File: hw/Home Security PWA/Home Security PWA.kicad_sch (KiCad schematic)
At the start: 46 parts, among them J1 Conn_01x10_Pin, J10 1884340000, J11 1884340000, J12 1884340000, J13 1884340000, J14 1884340000, J15 1884340000, J16 1884340000, J17 1884340000, J18 1884340000, J19 1884340000, J2 Conn_01x10_Pin, J20 1884340000, J21 1884340000, J22 1884340000, J23 1884340000, J24 1884340000, J25 1884340000, J26 1884340000, J27 1884340000, J28 1884340000, J29 1884340000, J3 1884340000, J30 1884340000, J4 1884340000, J5 1884340000, J6 1884340000, J7 1884340000, J8 1884340000, J9 1884340000, U1 ADS1115IDGS, U2 ADS1115IDGS, U3 MCP23017_SO

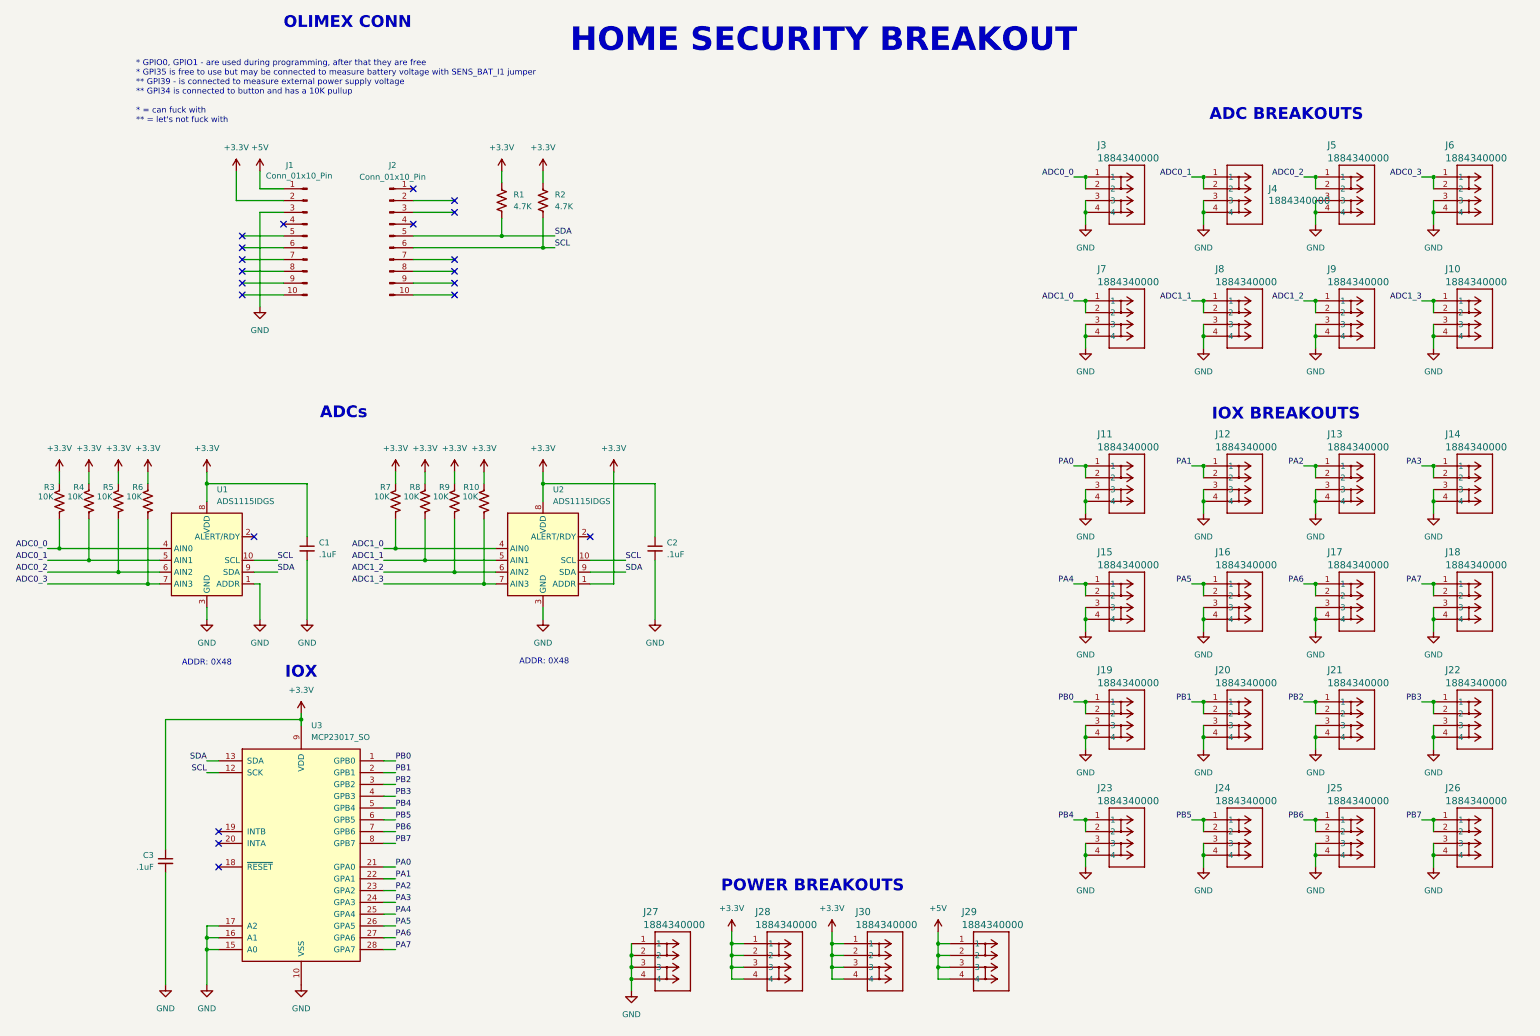
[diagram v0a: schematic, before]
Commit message: Rev A.
Added these "top" loader cable holders.
Added GPIOs that directly attach to the ESP32.
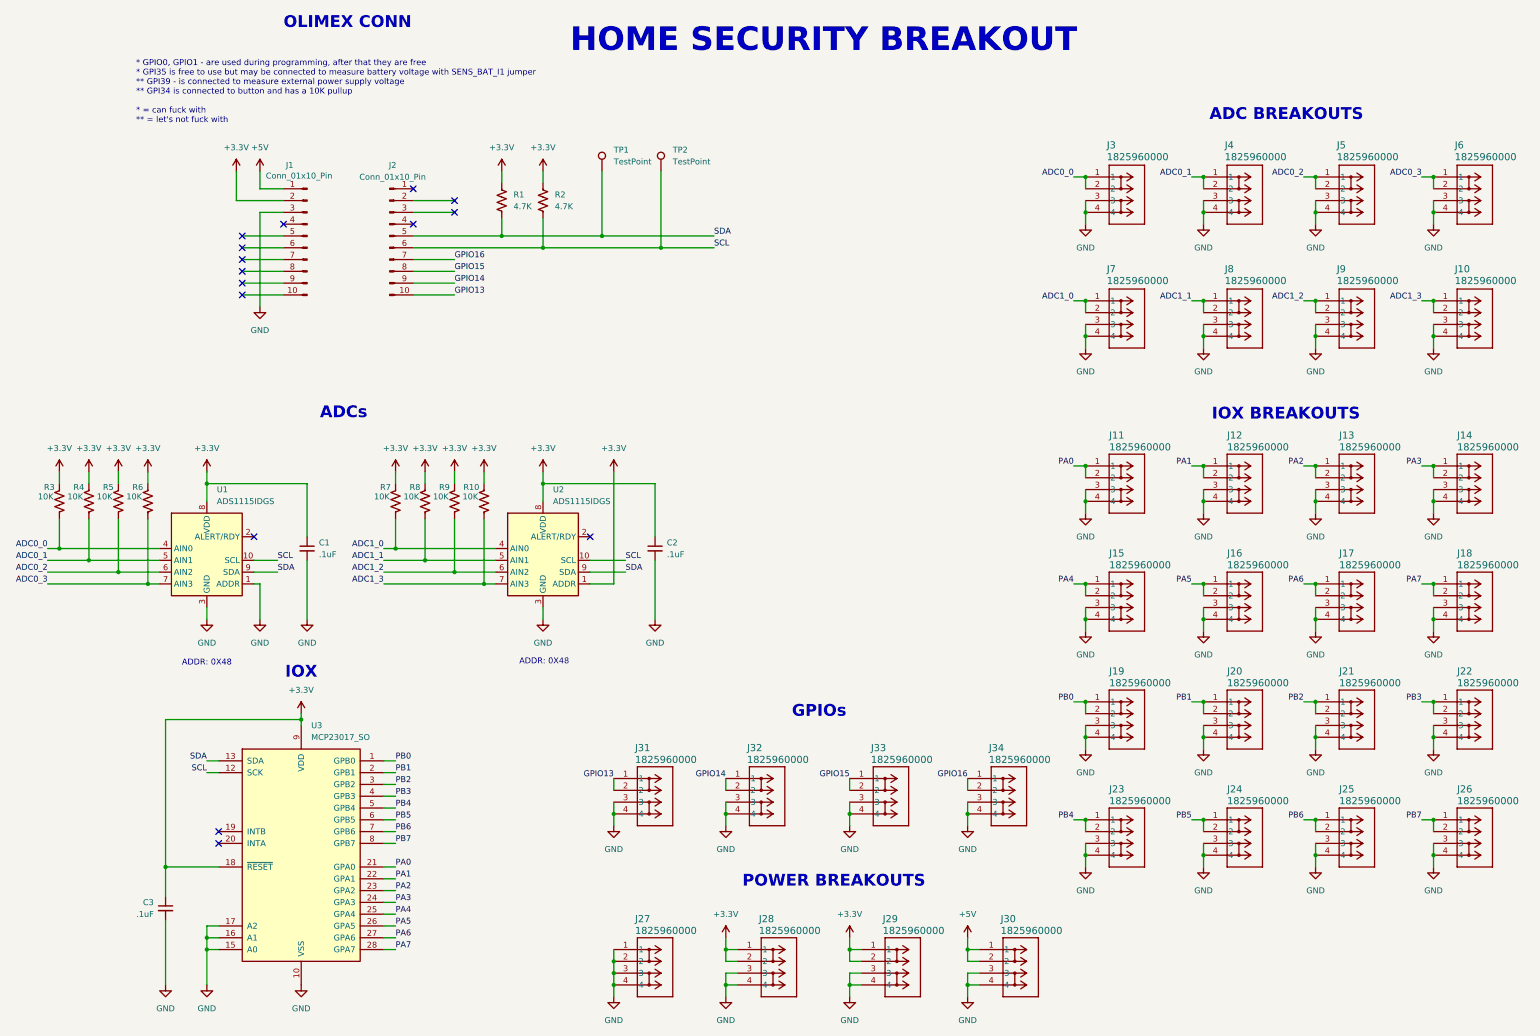
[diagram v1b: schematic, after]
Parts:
- removed J10, J11, J12, J13, J14, J15, J16, J17, J18, J19, J20, J21, J22, J23, J24, J25, J26, J27, J28, J29, J3, J30, J4, J5, J6, J7, J8, J9: 1884340000, footprint:CONN4_1884340000_WED, symbol 1884340000:1884340000
- added J10, J11, J12, J13, J14, J15, J16, J17, J18, J19, J20, J21, J22, J23, J24, J25, J26, J27, J28, J29, J3, J30, J31, J32, J33, J34, J4, J5, J6, J7, J8, J9: 1825960000, footprint:CONN_1825960000_WED, symbol 1825960000:1825960000
- added TP1, TP2: TestPoint, TestPoint:TestPoint_THTPad_D2.0mm_Drill1.0mm, symbol Connector:TestPoint
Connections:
- net +3.3V: now also U3.18 (~{RESET}), J28.1, J28.2, J29.1, J29.2
- net +5V: now also J30.1, J30.2
- net ADC0_0: now also J3.1, J3.2
- net ADC0_1: now also J4.1, J4.2
- net ADC0_2: now also J5.1, J5.2
- net ADC0_3: now also J6.1, J6.2
- net ADC1_0: now also J7.1, J7.2
- net ADC1_1: now also J8.1, J8.2
- net ADC1_2: now also J9.1, J9.2
- net ADC1_3: now also J10.1, J10.2
- net GND: now also J10.3, J10.4, J11.3, J11.4, J12.3, J12.4, J13.3, J13.4, J14.3, J14.4, J15.3, J15.4, J16.3, J16.4, J17.3, J17.4, J18.3, J18.4, J19.3, J19.4, J20.3, J20.4, J21.3, J21.4, J22.3, J22.4, J23.3, J23.4, J24.3, J24.4, J25.3, J25.4, J26.3, J26.4, J27.1, J27.2, J27.3, J27.4, J28.3, J28.4, J29.3, J29.4, J3.3, J3.4, J30.3, J30.4, J31.3, J31.4, J32.3, J32.4, J33.3, J33.4, J34.3, J34.4, J4.3, J4.4, J5.3, J5.4, J6.3, J6.4, J7.3, J7.4, J8.3, J8.4, J9.3, J9.4
- net PA0: now also J11.1, J11.2
- net PA1: now also J12.1, J12.2
- net PA2: now also J13.1, J13.2
- net PA3: now also J14.1, J14.2
- net PA4: now also J15.1, J15.2
- net PA5: now also J16.1, J16.2
- net PA6: now also J17.1, J17.2
- net PA7: now also J18.1, J18.2
- net PB0: now also J19.1, J19.2
- net PB1: now also J20.1, J20.2
- net PB2: now also J21.1, J21.2
- net PB3: now also J22.1, J22.2
- net PB4: now also J23.1, J23.2
- net PB5: now also J24.1, J24.2
- net PB6: now also J25.1, J25.2
- net PB7: now also J26.1, J26.2
- net SCL: now also TP2.1
- net SDA: now also TP1.1
- net GPIO13: now reaches J2.10 (Pin_10)
- net GPIO13: now also J31.1, J31.2
- net GPIO16: now reaches J2.7 (Pin_7)
- net GPIO16: now also J34.1, J34.2
- net GPIO15: now reaches J2.8 (Pin_8)
- net GPIO15: now also J33.1, J33.2
- net GPIO14: now reaches J2.9 (Pin_9)
- net GPIO14: now also J32.1, J32.2
- no-connect marks 20 -> 15
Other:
- note added: "GPIOs"
- moved on the sheet: C3
